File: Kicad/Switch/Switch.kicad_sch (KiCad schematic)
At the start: 15 parts, among them Q1 BD139, Q2 IXTH90P10P, Q4 BD139, Q5A1 BSC340N08NS3G, Q6 BD139

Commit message: update sockets
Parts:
- added J1, J2, J3: Conn_01x01_Socket, Connector_PinSocket_1.27mm:PinSocket_1x01_P1.27mm_Vertical, symbol Connector:Conn_01x01_Socket
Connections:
- net at Q2.3 (S), Q5A1.5 (D), R23.1: now also J3.1 (Pin_1)
- net +1V0: no longer names the net of Q1.2 (C), Q2.1 (D), R2.1
- net +1V0: now also J1.1 (Pin_1); no longer Q4.3 (B), R25.2
- new net: J2.1 (Pin_1), Q4.3 (B), R25.2
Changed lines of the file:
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@@
   (junction (at 157.48 116.84) (diameter 0) (color 0 0 0 0)
   )
+  (junction (at 182.88 104.14) (diameter 0) (color 0 0 0 0)
+  )
   (junction (at 121.92 139.7) (diameter 0) (color 0 0 0 0)
   )
@@
     (stroke (width 0) (type default))
   )
+  (wire (pts (xy 73.66 50.8) (xy 82.55 50.8))
+    (stroke (width 0) (type default))
+  )
   (wire (pts (xy 132.08 110.49) (xy 132.08 114.3))
     (stroke (width 0) (type default))
   )
-  (wire (pts (xy 73.66 48.26) (xy 73.66 50.8))
-    (stroke (width 0) (type default))
-  )
   (wire (pts (xy 182.88 135.89) (xy 182.88 140.97))
     (stroke (width 0) (type default))
@@
     (stroke (width 0) (type default))
   )
+  (wire (pts (xy 69.85 96.52) (xy 74.93 96.52))
+    (stroke (width 0) (type default))
+  )
   (wire (pts (xy 82.55 69.85) (xy 106.68 69.85))
     (stroke (width 0) (type default))
@@
     (stroke (width 0) (type default))
   )
-  (wire (pts (xy 68.58 96.52) (xy 74.93 96.52))
-    (stroke (width 0) (type default))
-  )
   (wire (pts (xy 182.88 123.19) (xy 182.88 128.27))
     (stroke (width 0) (type default))
@@
   )
   (wire (pts (xy 157.48 88.9) (xy 157.48 104.14))
-    (stroke (width 0) (type default))
-  )
-  (wire (pts (xy 73.66 50.8) (xy 82.55 50.8))
     (stroke (width 0) (type default))
   )
@@
     )
   )
+  (symbol (lib_id "Connector:Conn_01x01_Socket") (at 64.77 96.52 180) (unit 1)
+    (in_bom yes) (on_board yes) (dnp no) (fields_autoplaced)
+    (property "Reference" "J2" (at 65.405 91.44 0)
+      (effects (font (size 1.27 1.27)))
+    )
+    (property "Value" "Conn_01x01_Socket" (at 65.405 93.98 0)
+      (effects (font (size 1.27 1.27)))
+    )
+    (property "Footprint" "Connector_PinSocket_1.27mm:PinSocket_1x01_P1.27mm_Vertical" (at 64.77 96.52 0)
+      (effects (font (size 1.27 1.27)) hide)
+    )
+    (property "Datasheet" "~" (at 64.77 96.52 0)
+      (effects (font (size 1.27 1.27)) hide)
+    )
+    (pin "1")
+    (instances
+      (project "Switch"
+        (path "/4a9b42e5-b2d8-48b2-80cd-b93e35a2f77b"
+          (reference "J2") (unit 1)
+        )
+      )
+    )
+  )
   (symbol (lib_id "power:GND") (at 82.55 119.38 0) (unit 1)
     (in_bom yes) (on_board yes) (dnp no) (fields_autoplaced)
@@
     )
   )
+  (symbol (lib_id "Connector:Conn_01x01_Socket") (at 68.58 50.8 180) (unit 1)
+    (in_bom yes) (on_board yes) (dnp no) (fields_autoplaced)
+    (property "Reference" "J1" (at 69.215 45.72 0)
+      (effects (font (size 1.27 1.27)))
+    )
+    (property "Value" "Conn_01x01_Socket" (at 69.215 48.26 0)
+      (effects (font (size 1.27 1.27)))
+    )
+    (property "Footprint" "Connector_PinSocket_1.27mm:PinSocket_1x01_P1.27mm_Vertical" (at 68.58 50.8 0)
+      (effects (font (size 1.27 1.27)) hide)
+    )
+    (property "Datasheet" "~" (at 68.58 50.8 0)
+      (effects (font (size 1.27 1.27)) hide)
+    )
+    (pin "1")
+    (instances
+      (project "Switch"
+        (path "/4a9b42e5-b2d8-48b2-80cd-b93e35a2f77b"
+          (reference "J1") (unit 1)
+        )
+      )
+    )
+  )
   (symbol (lib_id "power:GND") (at 132.08 149.86 0) (unit 1)
     (in_bom yes) (on_board yes) (dnp no) (fields_autoplaced)
@@
     )
   )
-  (symbol (lib_id "power:+1V0") (at 73.66 48.26 0) (unit 1)
-    (in_bom yes) (on_board yes) (dnp no) (fields_autoplaced)
-    (property "Reference" "#PWR05" (at 73.66 52.07 0)
-      (effects (font (size 1.27 1.27)) hide)
-    )
-    (property "Value" "+1V0" (at 73.66 43.18 0)
-      (effects (font (size 1.27 1.27)))
-    )
-    (property "Footprint" "" (at 73.66 48.26 0)
-      (effects (font (size 1.27 1.27)) hide)
-    )
-    (property "Datasheet" "" (at 73.66 48.26 0)
-      (effects (font (size 1.27 1.27)) hide)
-    )
-    (pin "1")
-    (instances
-      (project "Switch"
-        (path "/4a9b42e5-b2d8-48b2-80cd-b93e35a2f77b"
-          (reference "#PWR05") (unit 1)
-        )
-      )
-    )
-  )
   (symbol (lib_id "Transistor_BJT:BD139") (at 111.76 69.85 0) (unit 1)
     (in_bom yes) (on_board yes) (dnp no) (fields_autoplaced)
@@
     )
   )
+  (symbol (lib_id "Connector:Conn_01x01_Socket") (at 187.96 104.14 0) (unit 1)
+    (in_bom yes) (on_board yes) (dnp no) (fields_autoplaced)
+    (property "Reference" "J3" (at 189.23 102.87 0)
+      (effects (font (size 1.27 1.27)) (justify left))
+    )
+    (property "Value" "Conn_01x01_Socket" (at 189.23 105.41 0)
+      (effects (font (size 1.27 1.27)) (justify left))
+    )
+    (property "Footprint" "Connector_PinSocket_1.27mm:PinSocket_1x01_P1.27mm_Vertical" (at 187.96 104.14 0)
+      (effects (font (size 1.27 1.27)) hide)
+    )
+    (property "Datasheet" "~" (at 187.96 104.14 0)
+      (effects (font (size 1.27 1.27)) hide)
+    )
+    (pin "1")
+    (instances
+      (project "Switch"
+        (path "/4a9b42e5-b2d8-48b2-80cd-b93e35a2f77b"
+          (reference "J3") (unit 1)
+        )
+      )
+    )
+  )
   (symbol (lib_id "Device:R") (at 104.14 118.11 0) (unit 1)
     (in_bom yes) (on_board yes) (dnp no) (fields_autoplaced)
@@
         )
       )
-    )
-  )
-  (symbol (lib_id "power:+1V0") (at 68.58 96.52 0) (unit 1)
-    (in_bom yes) (on_board yes) (dnp no) (fields_autoplaced)
-    (property "Reference" "#PWR06" (at 68.58 100.33 0)
-      (effects (font (size 1.27 1.27)) hide)
-    )
-    (property "Value" "+1V0" (at 68.58 91.44 0)
-      (effects (font (size 1.27 1.27)))
-    )
-    (property "Footprint" "" (at 68.58 96.52 0)
-      (effects (font (size 1.27 1.27)) hide)
-    )
-    (property "Datasheet" "" (at 68.58 96.52 0)
-      (effects (font (size 1.27 1.27)) hide)
-    )
-    (pin "1")
-    (instances
-      (project "Switch"
-        (path "/4a9b42e5-b2d8-48b2-80cd-b93e35a2f77b"
-          (reference "#PWR06") (unit 1)
-        )
-      )

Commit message: update ground plate
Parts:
- renumbered J1 to V56, J2 to VTackt, J3 to Vout
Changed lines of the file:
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@@
   (symbol (lib_id "Connector:Conn_01x01_Socket") (at 64.77 96.52 180) (unit 1)
     (in_bom yes) (on_board yes) (dnp no) (fields_autoplaced)
-    (property "Reference" "J2" (at 65.405 91.44 0)
+    (property "Reference" "VTackt" (at 65.405 91.44 0)
       (effects (font (size 1.27 1.27)))
     )
@@
       (project "Switch"
         (path "/4a9b42e5-b2d8-48b2-80cd-b93e35a2f77b"
-          (reference "J2") (unit 1)
+          (reference "VTackt") (unit 1)
         )
       )
@@
   (symbol (lib_id "Connector:Conn_01x01_Socket") (at 68.58 50.8 180) (unit 1)
     (in_bom yes) (on_board yes) (dnp no) (fields_autoplaced)
-    (property "Reference" "J1" (at 69.215 45.72 0)
+    (property "Reference" "V56" (at 69.215 45.72 0)
       (effects (font (size 1.27 1.27)))
     )
@@
       (project "Switch"
         (path "/4a9b42e5-b2d8-48b2-80cd-b93e35a2f77b"
-          (reference "J1") (unit 1)
+          (reference "V56") (unit 1)
         )
       )
@@
   (symbol (lib_id "Connector:Conn_01x01_Socket") (at 187.96 104.14 0) (unit 1)
     (in_bom yes) (on_board yes) (dnp no) (fields_autoplaced)
-    (property "Reference" "J3" (at 189.23 102.87 0)
+    (property "Reference" "Vout" (at 189.23 102.87 0)
       (effects (font (size 1.27 1.27)) (justify left))
     )
@@
       (project "Switch"
         (path "/4a9b42e5-b2d8-48b2-80cd-b93e35a2f77b"
-          (reference "J3") (unit 1)
-        )
-      )
+          (reference "Vout") (unit 1)
+        )
+      )

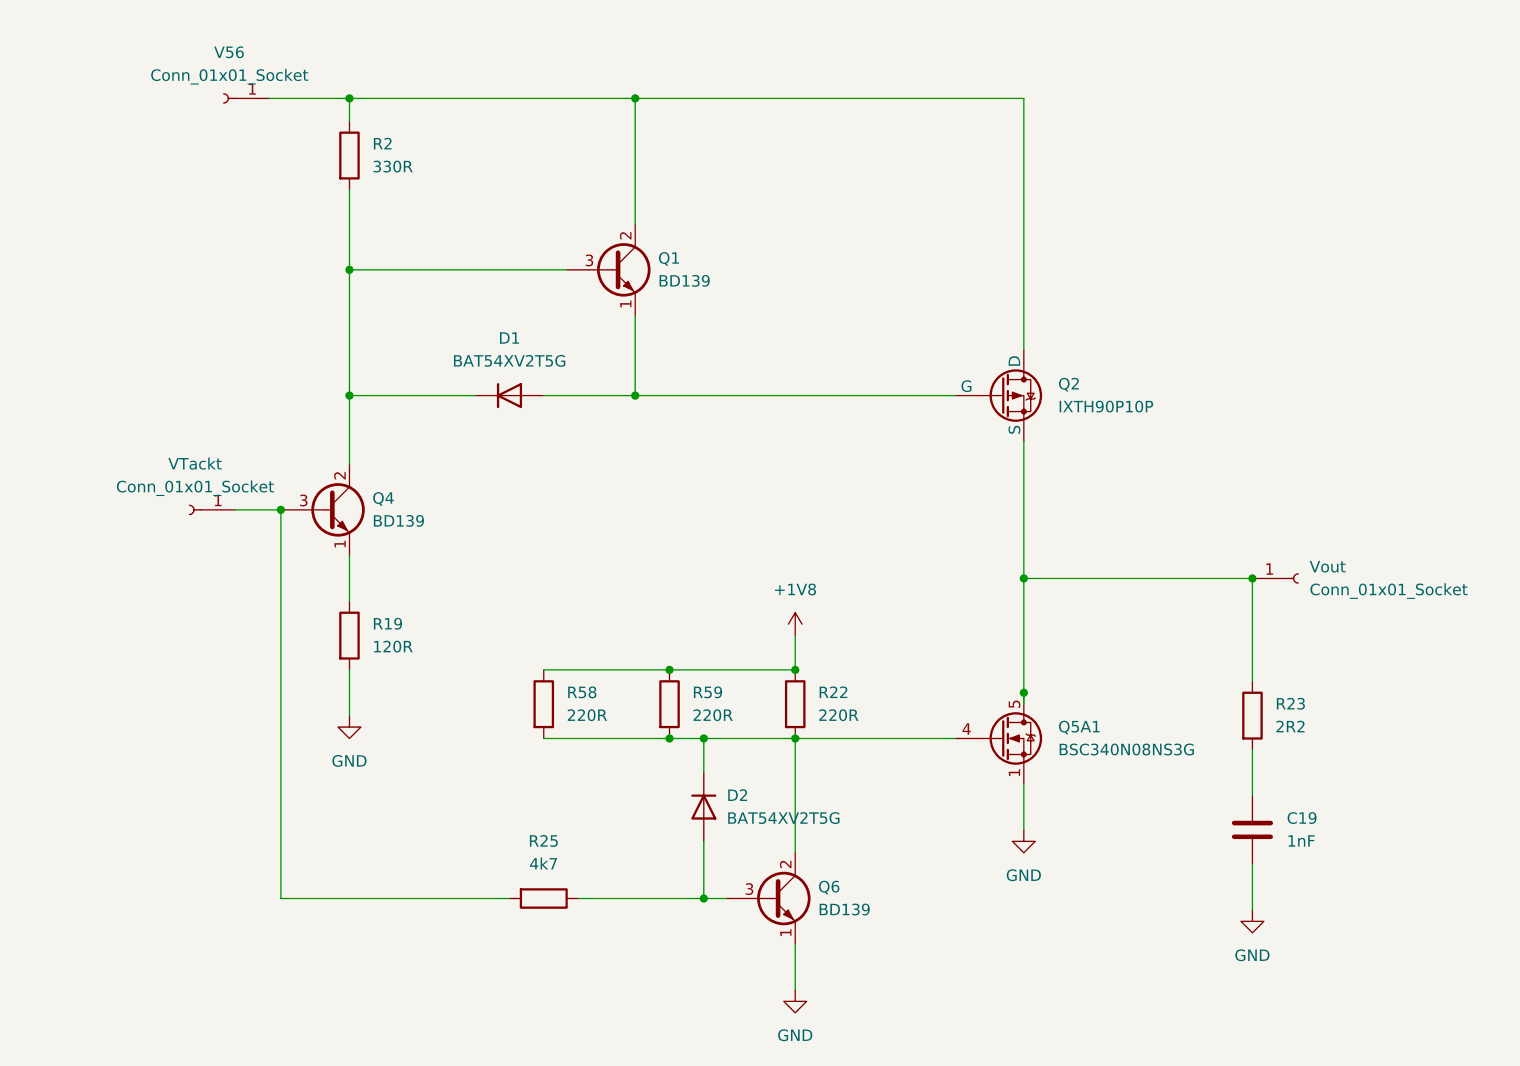
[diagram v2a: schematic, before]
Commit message: update vin/vout
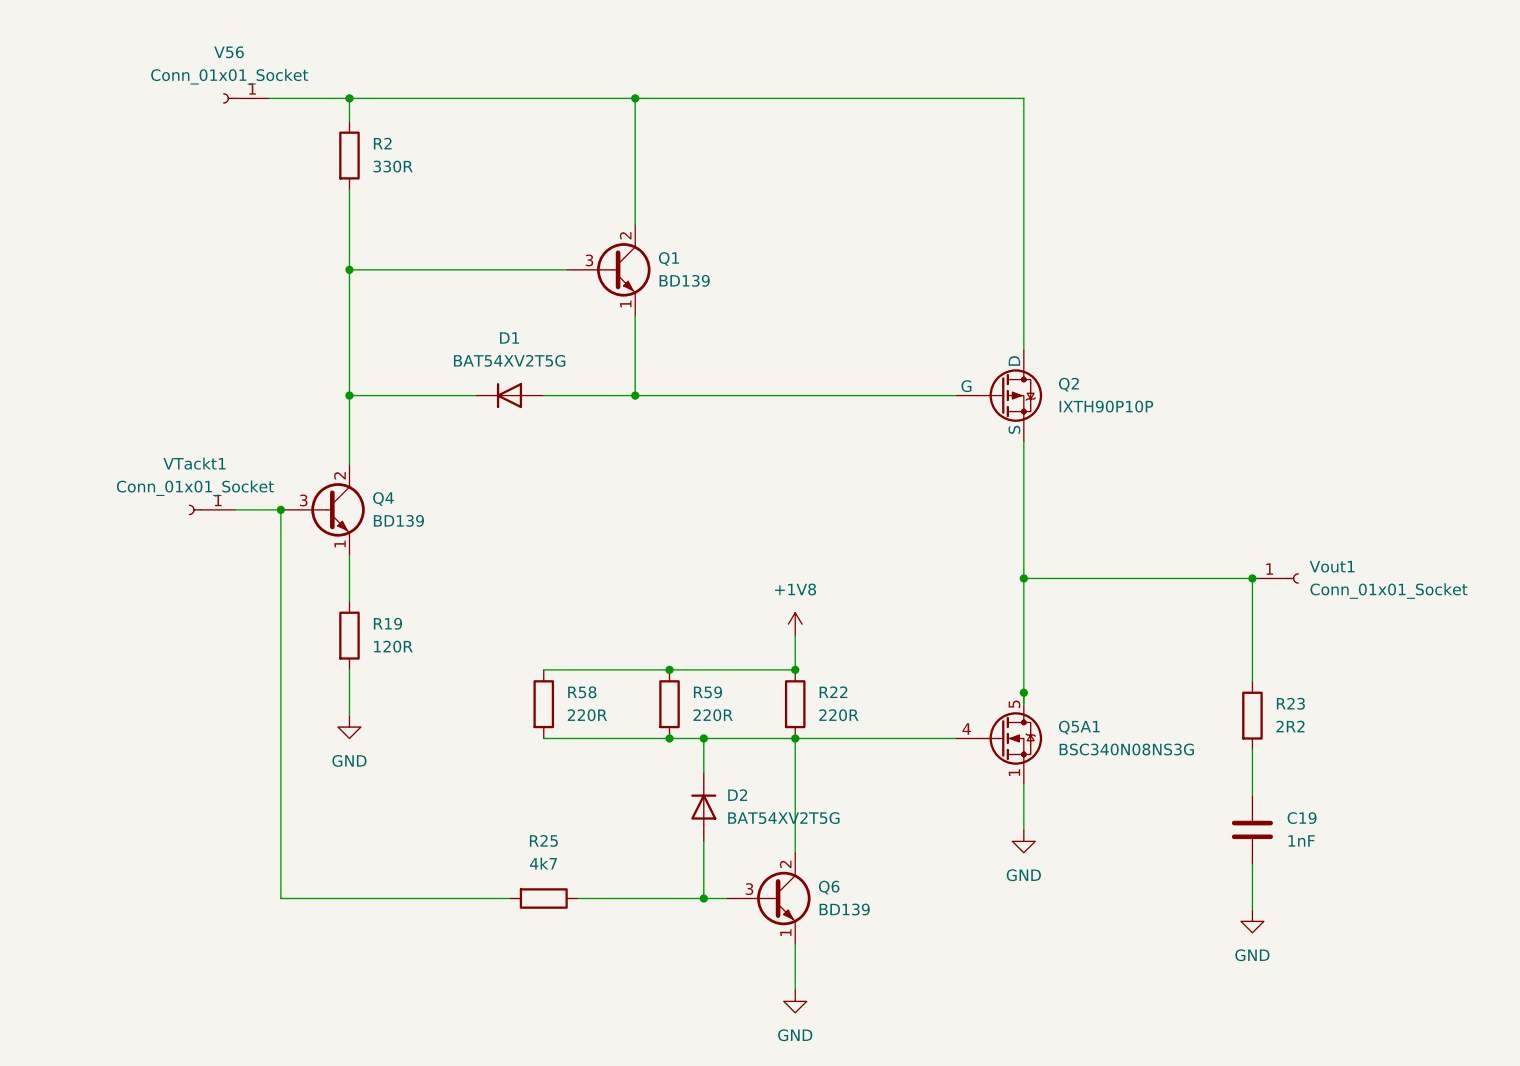
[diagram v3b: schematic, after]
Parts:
- renumbered VTackt to VTackt1, Vout to Vout1
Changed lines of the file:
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@@
   (symbol (lib_id "Connector:Conn_01x01_Socket") (at 64.77 96.52 180) (unit 1)
     (in_bom yes) (on_board yes) (dnp no) (fields_autoplaced)
-    (property "Reference" "VTackt" (at 65.405 91.44 0)
+    (property "Reference" "VTackt1" (at 65.405 91.44 0)
       (effects (font (size 1.27 1.27)))
     )
@@
       (project "Switch"
         (path "/4a9b42e5-b2d8-48b2-80cd-b93e35a2f77b"
-          (reference "VTackt") (unit 1)
+          (reference "VTackt1") (unit 1)
         )
       )
@@
   (symbol (lib_id "Connector:Conn_01x01_Socket") (at 187.96 104.14 0) (unit 1)
     (in_bom yes) (on_board yes) (dnp no) (fields_autoplaced)
-    (property "Reference" "Vout" (at 189.23 102.87 0)
+    (property "Reference" "Vout1" (at 189.23 102.87 0)
       (effects (font (size 1.27 1.27)) (justify left))
     )
@@
       (project "Switch"
         (path "/4a9b42e5-b2d8-48b2-80cd-b93e35a2f77b"
-          (reference "Vout") (unit 1)
-        )
-      )
+          (reference "Vout1") (unit 1)
+        )
+      )

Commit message: Vp1 socket
install Vp1 socket
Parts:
- added V8: Conn_01x01_Socket, Connector_PinSocket_1.27mm:PinSocket_1x01_P1.27mm_Vertical, symbol Connector:Conn_01x01_Socket
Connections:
- net +1V8: no longer names the net of R22.1, R58.1, R59.1
- net +1V8: now also V8.1 (Pin_1)
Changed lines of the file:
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@@
   (junction (at 82.55 69.85) (diameter 0) (color 0 0 0 0)
   )
-  (junction (at 132.08 114.3) (diameter 0) (color 0 0 0 0)
-  )
   (junction (at 118.11 114.3) (diameter 0) (color 0 0 0 0)
   )
   (junction (at 132.08 121.92) (diameter 0) (color 0 0 0 0)
   )
+  (junction (at 128.27 114.3) (diameter 0) (color 0 0 0 0)
+  )
   (junction (at 114.3 50.8) (diameter 0) (color 0 0 0 0)
   )
@@
     (stroke (width 0) (type default))
   )
-  (wire (pts (xy 132.08 110.49) (xy 132.08 114.3))
-    (stroke (width 0) (type default))
-  )
   (wire (pts (xy 182.88 135.89) (xy 182.88 140.97))
     (stroke (width 0) (type default))
@@
     (stroke (width 0) (type default))
   )
-  (wire (pts (xy 118.11 114.3) (xy 132.08 114.3))
+  (wire (pts (xy 118.11 114.3) (xy 128.27 114.3))
     (stroke (width 0) (type default))
   )
@@
   )
   (wire (pts (xy 118.11 121.92) (xy 121.92 121.92))
+    (stroke (width 0) (type default))
+  )
+  (wire (pts (xy 128.27 114.3) (xy 132.08 114.3))
     (stroke (width 0) (type default))
   )
@@
     )
   )
-  (symbol (lib_id "power:+1V8") (at 132.08 110.49 0) (unit 1)
-    (in_bom yes) (on_board yes) (dnp no) (fields_autoplaced)
-    (property "Reference" "#PWR07" (at 132.08 114.3 0)
-      (effects (font (size 1.27 1.27)) hide)
-    )
-    (property "Value" "+1V8" (at 132.08 105.41 0)
-      (effects (font (size 1.27 1.27)))
-    )
-    (property "Footprint" "" (at 132.08 110.49 0)
-      (effects (font (size 1.27 1.27)) hide)
-    )
-    (property "Datasheet" "" (at 132.08 110.49 0)
-      (effects (font (size 1.27 1.27)) hide)
-    )
-    (pin "1")
-    (instances
-      (project "Switch"
-        (path "/4a9b42e5-b2d8-48b2-80cd-b93e35a2f77b"
-          (reference "#PWR07") (unit 1)
-        )
-      )
+  (symbol (lib_id "Connector:Conn_01x01_Socket") (at 128.27 109.22 90) (unit 1)
+    (in_bom yes) (on_board yes) (dnp no) (fields_autoplaced)
+    (property "Reference" "V8" (at 129.54 108.585 90)
+      (effects (font (size 1.27 1.27)) (justify right))
+    )
+    (property "Value" "Conn_01x01_Socket" (at 129.54 111.125 90)
+      (effects (font (size 1.27 1.27)) (justify right))
+    )
+    (property "Footprint" "Connector_PinSocket_1.27mm:PinSocket_1x01_P1.27mm_Vertical" (at 128.27 109.22 0)
+      (effects (font (size 1.27 1.27)) hide)
+    )
+    (property "Datasheet" "~" (at 128.27 109.22 0)
+      (effects (font (size 1.27 1.27)) hide)
+    )
+    (pin "1")
+    (instances
+      (project "Switch"
+        (path "/4a9b42e5-b2d8-48b2-80cd-b93e35a2f77b"
+          (reference "V8") (unit 1)
+        )
+      )

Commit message: update
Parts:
- added J1: Conn_01x01, Connector:Banana_Jack_1Pin, symbol Connector_Generic:Conn_01x01
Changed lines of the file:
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@@
+    )
+  )
+  (symbol (lib_id "Connector_Generic:Conn_01x01") (at 50.8 54.61 0) (unit 1)
+    (in_bom yes) (on_board yes) (dnp no) (fields_autoplaced)
+    (property "Reference" "J1" (at 53.34 53.34 0)
+      (effects (font (size 1.27 1.27)) (justify left))
+    )
+    (property "Value" "Conn_01x01" (at 53.34 55.88 0)
+      (effects (font (size 1.27 1.27)) (justify left))
+    )
+    (property "Footprint" "Connector:Banana_Jack_1Pin" (at 50.8 54.61 0)
+      (effects (font (size 1.27 1.27)) hide)
+    )
+    (property "Datasheet" "~" (at 50.8 54.61 0)
+      (effects (font (size 1.27 1.27)) hide)
+    )
+    (pin "1")
+    (instances
+      (project "Switch"
+        (path "/4a9b42e5-b2d8-48b2-80cd-b93e35a2f77b"
+          (reference "J1") (unit 1)
+        )
+      )
     )
   )
